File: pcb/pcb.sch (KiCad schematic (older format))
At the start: 39 parts, among them J1 USB_B_Mini, J4 UART_BUS, Q1 BSS138DW-7-F, SW1 PTS645Vx83, SW2 PTS645Vx83, SW3 PTS645Vx83, SW4 KMR2, U1 AP2112K-3.3, U2 MIC5225-1.8YM5, U3 CP2104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

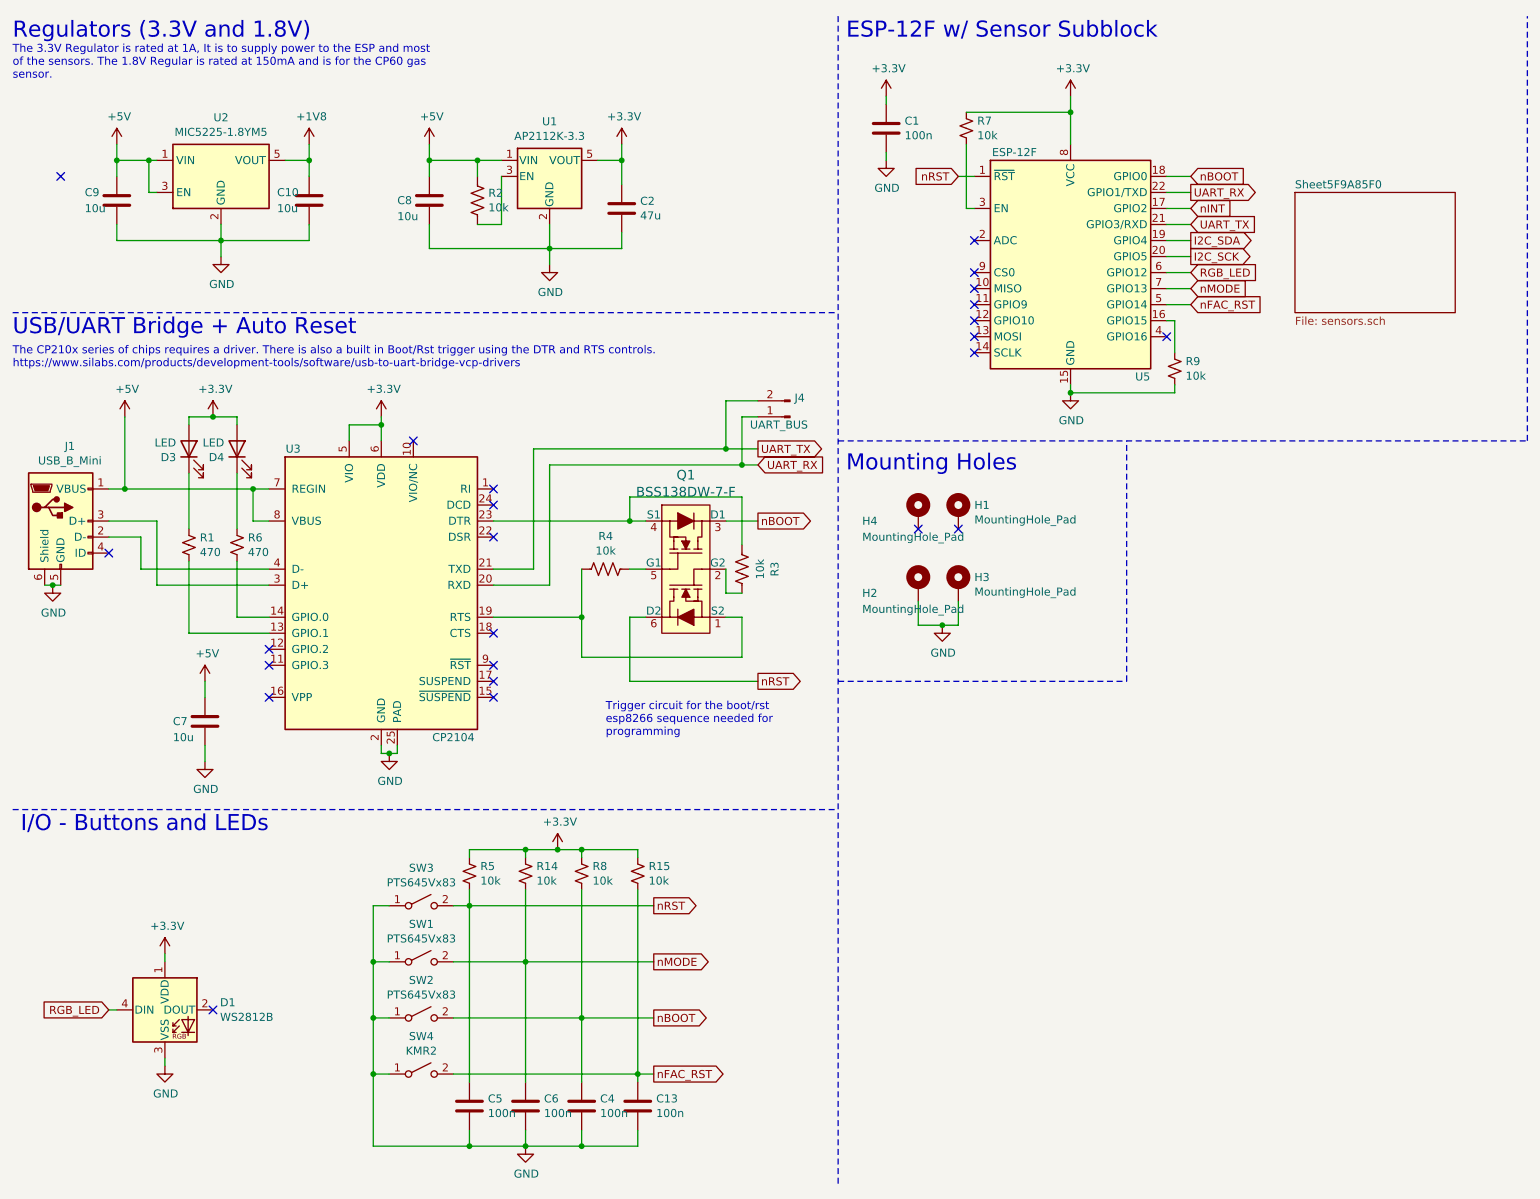
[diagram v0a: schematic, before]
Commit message: use the right tsl2591 footprint
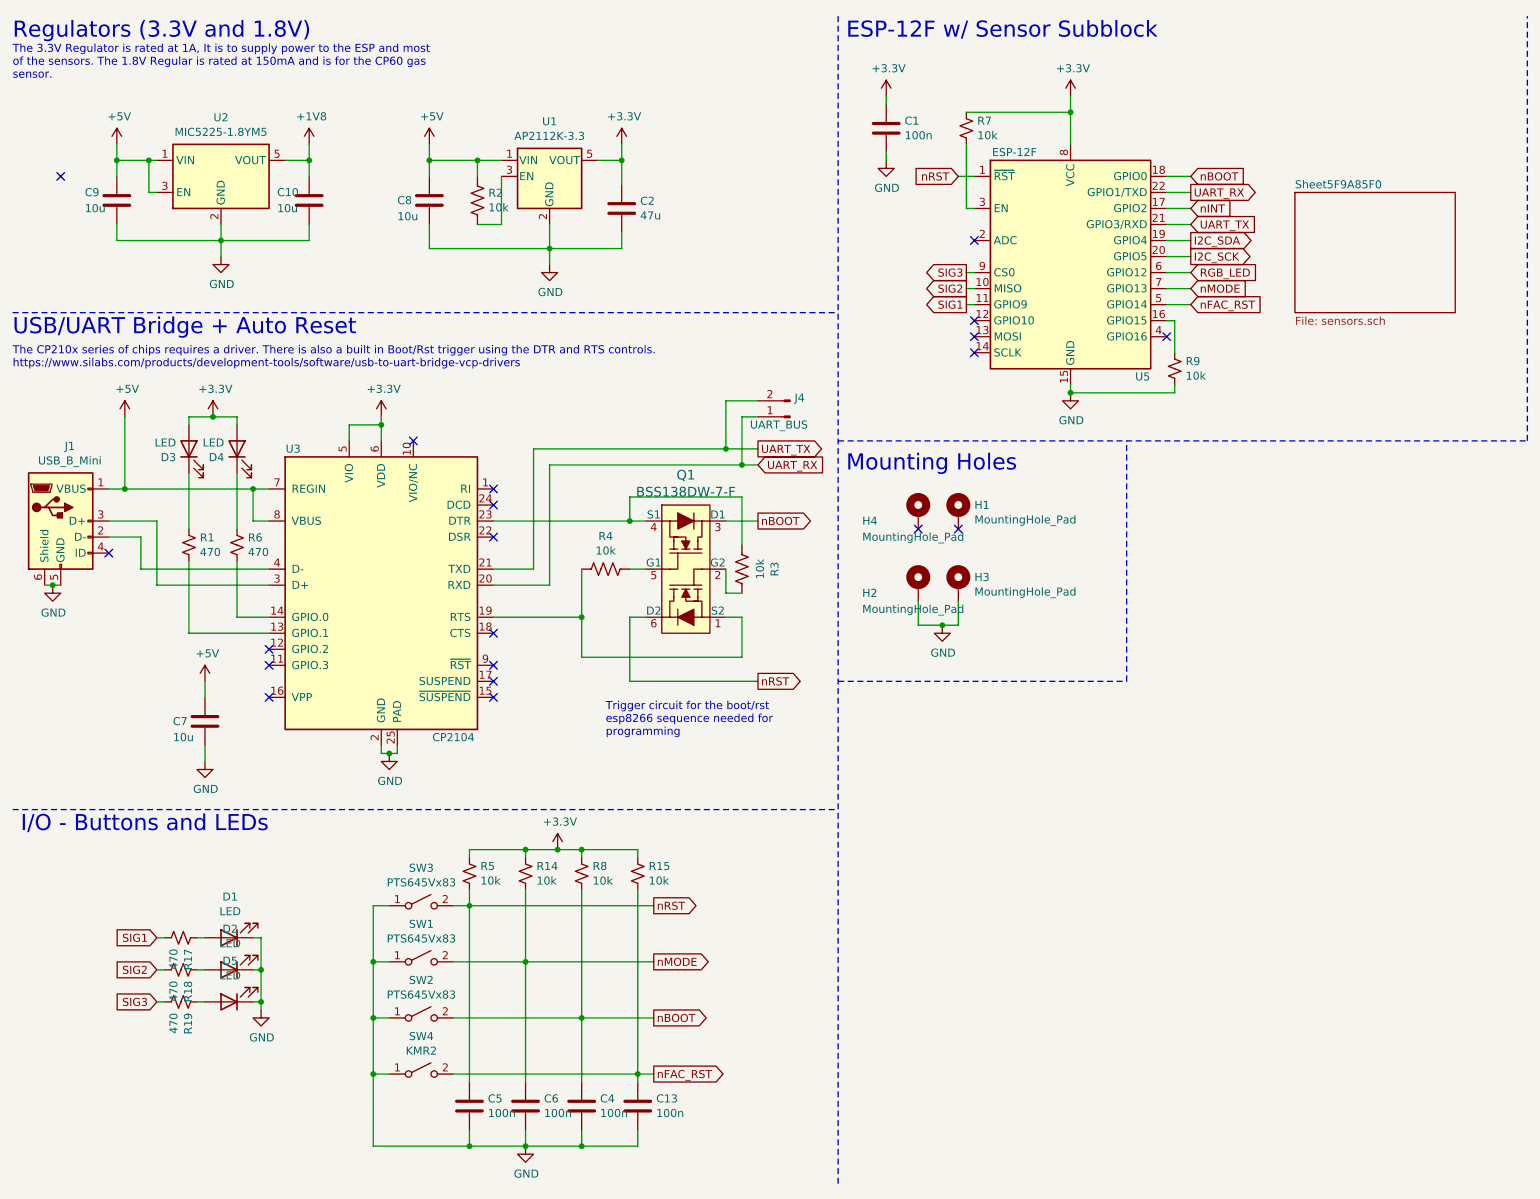
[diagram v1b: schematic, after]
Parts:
- removed D1: WS2812B, LED_SMD:LED_WS2812B_PLCC4_5.0x5.0mm_P3.2mm, symbol LED:WS2812B
- added D1, D2, D5: LED, LED_SMD:LED_0603_1608Metric, symbol Device:LED
- added R17, R18, R19: 470, Resistor_SMD:R_0603_1608Metric, symbol Device:R_Small_US
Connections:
- net GND: now also D1.1 (K), D2.1 (K), D5.1 (K)
- net SIG2: now reaches U5.10 (MISO)
- net SIG2: now also R18.2
- net SIG1: now reaches U5.11 (GPIO9)
- net SIG1: now also R17.2
- net SIG3: now reaches U5.9 (CS0)
- net SIG3: now also R19.2
- new net: D1.2 (A), R17.1
- new net: D2.2 (A), R18.1
- new net: D5.2 (A), R19.1
- no-connect marks 24 -> 20
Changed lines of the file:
@@
 NoConn ~ 3500 3550
 NoConn ~ 3500 3450
-NoConn ~ 6500 2300
 NoConn ~ 6500 2400
 Wire Notes Line
@@
 	1    0    0    -1
 $EndComp
-$Comp
-L power:+3.3V #PWR0123
-U 1 1 5F4FBB06
-P 1450 6350
-F 0 "#PWR0123" H 1450 6200 50  0001 C CNN
-F 1 "+3.3V" H 1465 6523 50  0000 C CNN
-F 2 "" H 1450 6350 50  0001 C CNN
-F 3 "" H 1450 6350 50  0001 C CNN
-	1    1450 6350
-	1    0    0    -1
-$EndComp
-$Comp
-L power:GND #PWR0132
-U 1 1 5F4FC014
-P 1450 7050
-F 0 "#PWR0132" H 1450 6800 50  0001 C CNN
-F 1 "GND" H 1455 6877 50  0000 C CNN
-F 2 "" H 1450 7050 50  0001 C CNN
-F 3 "" H 1450 7050 50  0001 C CNN
-	1    1450 7050
-	1    0    0    -1
-$EndComp
-Wire Wire Line
-	1450 6400 1450 6350
-Wire Wire Line
-	1450 7000 1450 7050
-$Comp
-L LED:WS2812B D1
-U 1 1 5F529F39
-P 1450 6700
-F 0 "D1" H 1794 6746 50  0000 L CNN
-F 1 "WS2812B" H 1794 6655 50  0000 L CNN
-F 2 "LED_SMD:LED_WS2812B_PLCC4_5.0x5.0mm_P3.2mm" H 1500 6400 50  0001 L TNN
-F 3 "https://cdn-shop.adafruit.com/datasheets/WS2812B.pdf" H 1550 6325 50  0001 L TNN
-	1    1450 6700
-	1    0    0    -1
-$EndComp
-Text GLabel 1100 6700 0    50   Input ~ 0
-RGB_LED
-Wire Wire Line
-	1100 6700 1150 6700
 Wire Wire Line
 	4500 6400 3700 6400
@@
 Text GLabel 7850 2200 2    50   Input ~ 0
 nMODE
-NoConn ~ 1750 6700
 NoConn ~ 3000 3150
 Text GLabel 7850 1700 2    50   Input ~ 0
@@
 	7700 1700 7850 1700
 NoConn ~ 7700 2500
-NoConn ~ 6500 2100
-NoConn ~ 6500 2200
 NoConn ~ 6500 2600
 Connection ~ 4300 1400
@@
 	1    0    0    -1
 $EndComp
+$Comp
+L Device:LED D1
+U 1 1 5FFB8848
+P 1850 6250
+F 0 "D1" H 1843 5995 50  0000 C CNN
+F 1 "LED" H 1843 6086 50  0000 C CNN
+F 2 "LED_SMD:LED_0603_1608Metric" H 1850 6250 50  0001 C CNN
+F 3 "~" H 1850 6250 50  0001 C CNN
+	1    1850 6250
+	-1   0    0    1
+$EndComp
+$Comp
+L Device:LED D2
+U 1 1 5FFB92C8
+P 1850 6450
+F 0 "D2" H 1843 6195 50  0000 C CNN
+F 1 "LED" H 1843 6286 50  0000 C CNN
+F 2 "LED_SMD:LED_0603_1608Metric" H 1850 6450 50  0001 C CNN
+F 3 "~" H 1850 6450 50  0001 C CNN
+	1    1850 6450
+	-1   0    0    1
+$EndComp
+$Comp
+L Device:LED D5
+U 1 1 5FFB9A43
+P 1850 6650
+F 0 "D5" H 1843 6395 50  0000 C CNN
+F 1 "LED" H 1843 6486 50  0000 C CNN
+F 2 "LED_SMD:LED_0603_1608Metric" H 1850 6650 50  0001 C CNN
+F 3 "~" H 1850 6650 50  0001 C CNN
+	1    1850 6650
+	-1   0    0    1
+$EndComp
+$Comp
+L Device:R_Small_US R17
+U 1 1 5FFBA97E
+P 1550 6250
+F 0 "R17" H 1618 6296 50  0000 L CNN
+F 1 "470" H 1618 6205 50  0000 L CNN
+F 2 "Resistor_SMD:R_0603_1608Metric" H 1550 6250 50  0001 C CNN
+F 3 "~" H 1550 6250 50  0001 C CNN
+	1    1550 6250
+	0    1    1    0
+$EndComp
+$Comp
+L Device:R_Small_US R18
+U 1 1 5FFBB322
+P 1550 6450
+F 0 "R18" H 1618 6496 50  0000 L CNN
+F 1 "470" H 1618 6405 50  0000 L CNN
+F 2 "Resistor_SMD:R_0603_1608Metric" H 1550 6450 50  0001 C CNN
+F 3 "~" H 1550 6450 50  0001 C CNN
+	1    1550 6450
+	0    1    1    0
+$EndComp
+$Comp
+L Device:R_Small_US R19
+U 1 1 5FFBB8C2
+P 1550 6650
+F 0 "R19" H 1618 6696 50  0000 L CNN
+F 1 "470" H 1618 6605 50  0000 L CNN
+F 2 "Resistor_SMD:R_0603_1608Metric" H 1550 6650 50  0001 C CNN
+F 3 "~" H 1550 6650 50  0001 C CNN
+	1    1550 6650
+	0    1    1    0
+$EndComp
+$Comp
+L power:GND #PWR0101
+U 1 1 5FFBBD6A
+P 2050 6700
+F 0 "#PWR0101" H 2050 6450 50  0001 C CNN
+F 1 "GND" H 2055 6527 50  0000 C CNN
+F 2 "" H 2050 6700 50  0001 C CNN
+F 3 "" H 2050 6700 50  0001 C CNN
+	1    2050 6700
+	1    0    0    -1
+$EndComp
+Wire Wire Line
+	2000 6250 2050 6250
+Wire Wire Line
+	2050 6250 2050 6450
+Wire Wire Line
+	2000 6650 2050 6650
+Connection ~ 2050 6650
+Wire Wire Line
+	2050 6650 2050 6700
+Wire Wire Line
+	2000 6450 2050 6450
+Connection ~ 2050 6450
+Wire Wire Line
+	2050 6450 2050 6650
+Wire Wire Line
+	1650 6250 1700 6250
+Wire Wire Line
+	1650 6450 1700 6450
+Wire Wire Line
+	1650 6650 1700 6650
+Text GLabel 1400 6250 0    50   Input ~ 0
+SIG1
+Text GLabel 1400 6450 0    50   Input ~ 0
+SIG2
+Text GLabel 1400 6650 0    50   Input ~ 0
+SIG3
+Wire Wire Line
+	1400 6250 1450 6250
+Wire Wire Line
+	1400 6450 1450 6450
+Wire Wire Line
+	1400 6650 1450 6650
+Text GLabel 6450 2100 0    50   Output ~ 0
+SIG3
+Text GLabel 6450 2200 0    50   Output ~ 0
+SIG2
+Text GLabel 6450 2300 0    50   Output ~ 0
+SIG1
+Wire Wire Line
+	6450 2100 6500 2100
+Wire Wire Line
+	6450 2200 6500 2200
+Wire Wire Line
+	6450 2300 6500 2300
 $EndSCHEMATC

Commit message: cleaning up logic
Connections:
- net RGB_LED: no longer names the net of U5.6 (GPIO12)
- no-connect marks 20 -> 21
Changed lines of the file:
@@
 Wire Wire Line
 	3500 3650 4350 3650
-Text GLabel 7850 2100 2    50   Input ~ 0
-RGB_LED
-Wire Wire Line
-	7700 2100 7850 2100
 Wire Wire Line
 	7700 1700 7850 1700
@@
 F 3 "~" H 4300 1700 50  0001 C CNN
 	1    4300 1700
-	1    0    0    -1
-$EndComp
-$Comp
-L Regulator_Linear:AP2112K-3.3 U1
-U 1 1 5F256A82
-P 3850 1500
-F 0 "U1" H 3850 1842 50  0000 C CNN
-F 1 "AP2112K-3.3" H 3850 1751 50  0000 C CNN
-F 2 "Package_TO_SOT_SMD:SOT-23-5" H 3850 1825 50  0001 C CNN
-F 3 "https://www.diodes.com/assets/Datasheets/AP2112.pdf" H 3850 1600 50  0001 C CNN
-	1    3850 1500
 	1    0    0    -1
 $EndComp
@@
 Wire Wire Line
 	6450 2300 6500 2300
+$Comp
+L Regulator_Linear:AP2112K-3.3 U1
+U 1 1 5F256A82
+P 3850 1500
+F 0 "U1" H 3850 1842 50  0000 C CNN
+F 1 "AP2112K-3.3" H 3850 1751 50  0000 C CNN
+F 2 "Package_TO_SOT_SMD:SOT-23-5" H 3850 1825 50  0001 C CNN
+F 3 "https://www.diodes.com/assets/Datasheets/AP2112.pdf" H 3850 1600 50  0001 C CNN
+	1    3850 1500
+	1    0    0    -1
+$EndComp
+NoConn ~ 7700 2100
 $EndSCHEMATC
